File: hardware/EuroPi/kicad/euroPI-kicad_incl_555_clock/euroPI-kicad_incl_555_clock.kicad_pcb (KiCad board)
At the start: 2 copper layers, 121.9 x 128.5 mm, 104 parts, among them J1 Output 1 Jack, J10 Eurorack Power 2x8 16p, J11 Conn_01x13_Socket, J12 OLED 64x128, J13 USB_B_Micro, J14 Conn_01x03_Pin, J15 Conn_01x04_Pin, J16 Conn_02x04_Top_Bottom, J17 Conn_01x13_Pin, J18 Conn_01x04_Pin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

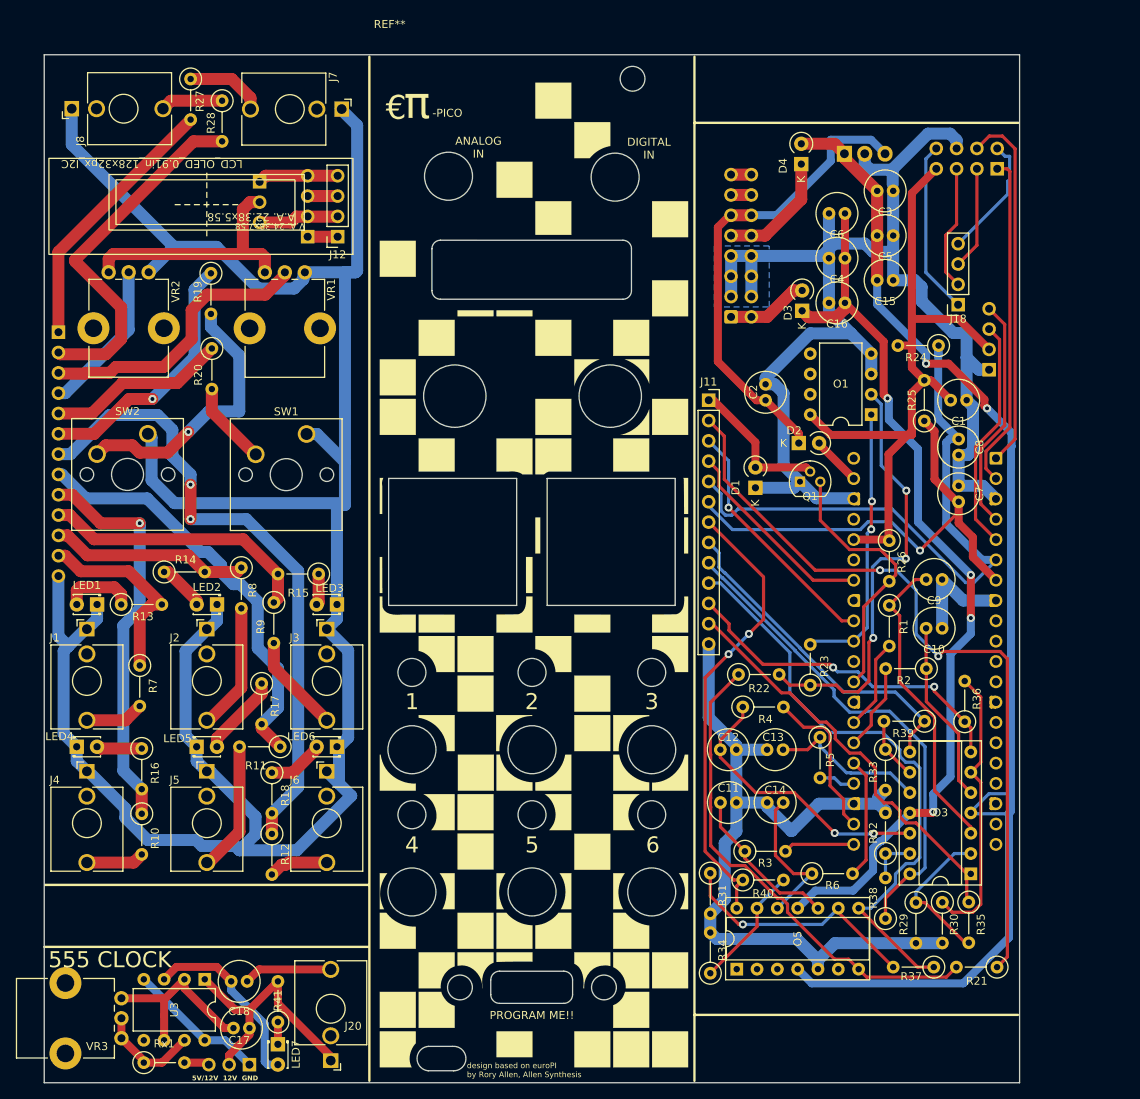
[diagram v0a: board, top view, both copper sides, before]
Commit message: THT version updated with ground plane
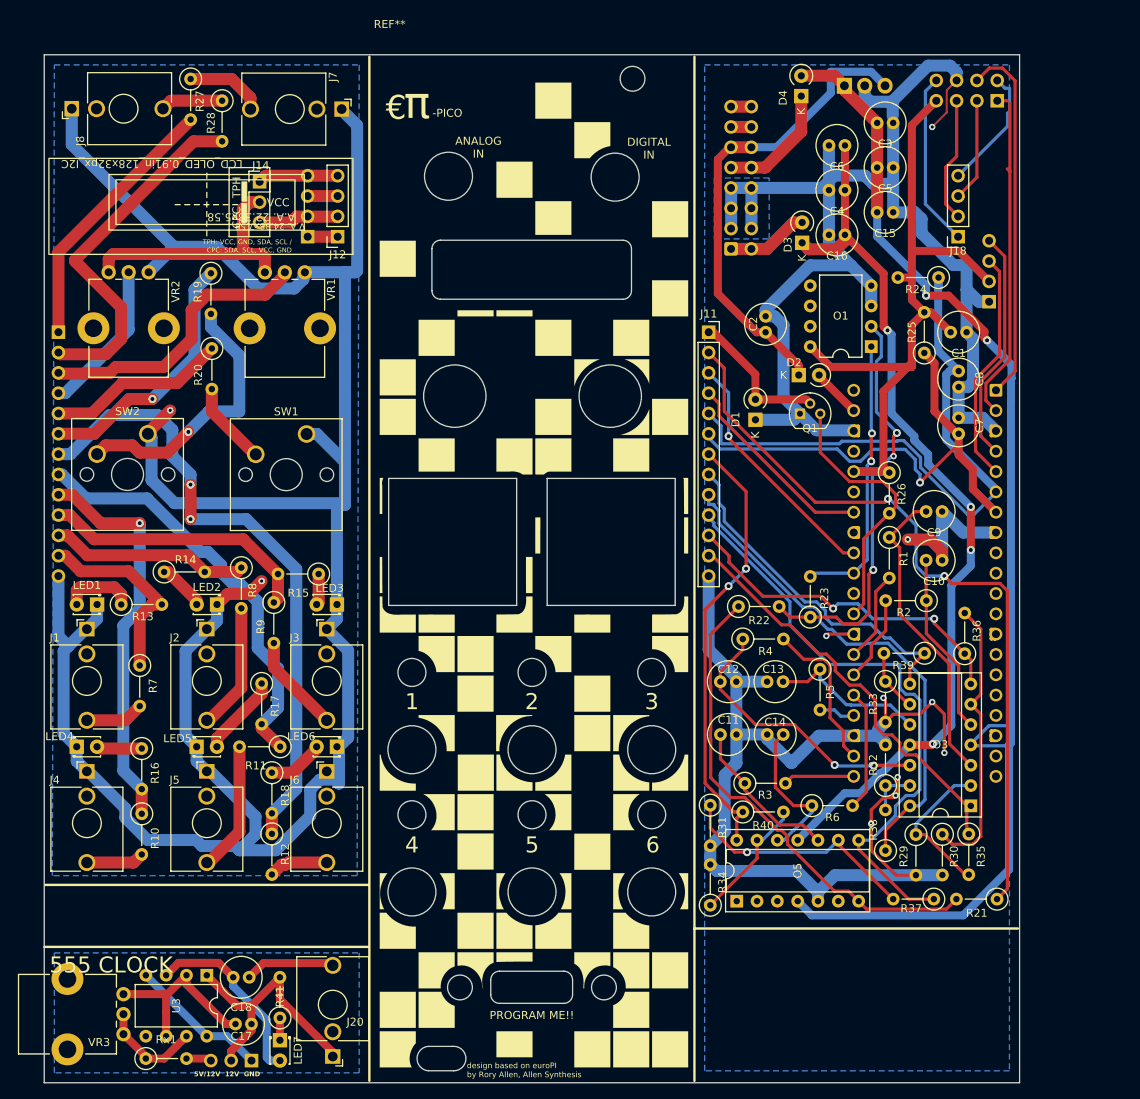
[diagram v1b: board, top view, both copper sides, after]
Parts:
- J14: moved to F.Cu
- moved R38 8.50 mm to (186.4, 124.9)
- moved R40 8.50 mm to (168.6, 120.1)
- moved R25 8.50 mm to (191.3, 62.7)
- moved D4 8.50 mm to (175.9, 30.6)
- moved U1 8.50 mm to (181.3, 29.3)
- moved C1 8.50 mm to (194.6, 60.1)
- moved C10 8.50 mm to (191.5, 88.6)
- moved C11 8.50 mm to (165.8, 110.4)
- moved C12 8.50 mm to (165.8, 103.8)
- moved C13 8.50 mm to (173.6, 103.8)
- moved C14 8.50 mm to (173.7, 110.4)
- moved C15 8.50 mm to (185.4, 45.1)
- moved C16 8.50 mm to (179.4, 47.9)
- moved C2 8.50 mm to (171.4, 60.1)
- moved C3 8.50 mm to (185.4, 33.9)
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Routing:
- net I2C_GND: track 610.0 -> 671.9 mm, vias 0 -> 11
- net I2C_VCC: track 117.6 -> 121.8 mm
- net Net-(O1A--): track 54.2 -> 52.0 mm
- net CJ6: track 136.6 -> 134.5 mm
- net CS2: track 94.2 -> 95.9 mm
- net CJ5: track 95.0 -> 96.6 mm
- net -12V: track 114.9 -> 113.3 mm
- net CJ4: track 111.3 -> 112.9 mm
- net CJ3: track 108.3 -> 109.4 mm
- net CS1: track 100.5 -> 100.0 mm
- net Net-(O5D-+): track 18.6 -> 19.1 mm

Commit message: wip tried a reroute should move power rail caps closer i think
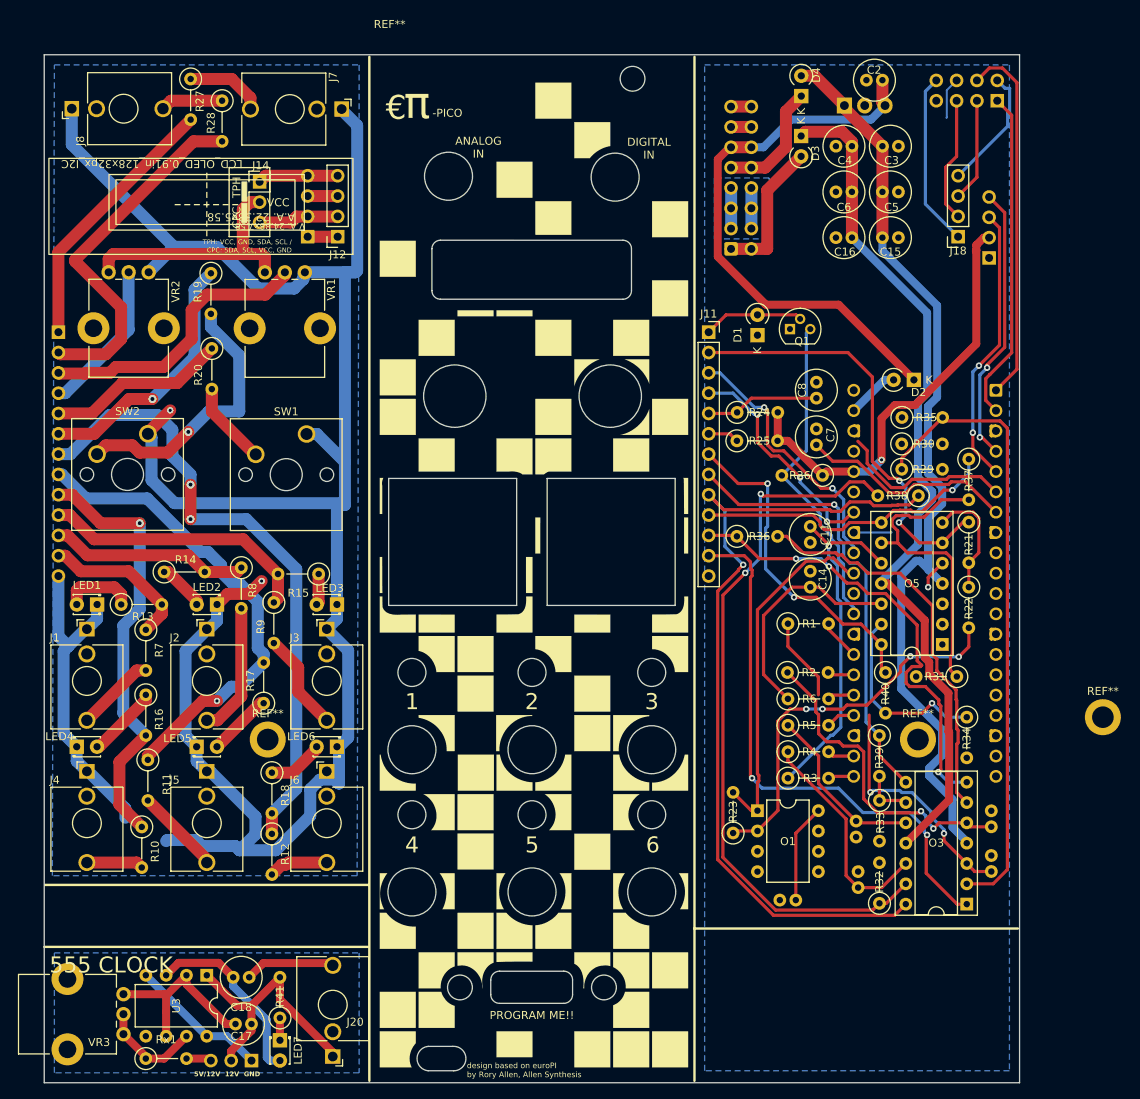
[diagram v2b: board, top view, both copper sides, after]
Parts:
- added REF**: MountingHole_2.7mm_M2.5_ISO14580_Pad, MountingHole:MountingHole_2.7mm_M2.5_ISO14580_Pad, F.Cu at (109.2, 111.0)
- added REF**: MountingHole_2.7mm_M2.5_ISO14580_Pad, MountingHole:MountingHole_2.7mm_M2.5_ISO14580_Pad, F.Cu at (213.6, 108.2)
- added REF**: MountingHole_2.7mm_M2.5_ISO14580_Pad, MountingHole:MountingHole_2.7mm_M2.5_ISO14580_Pad, F.Cu at (190.5, 111.0)
- C1, C10, C12, C13, C9: moved to B.Cu
- D1, D2, D3, D4: value type="D" model="DIODE" lib="" -> 1n4001
- moved C1 73.6 mm to (175.2, 131.1), turned to 180 degrees
- moved O1 59.7 mm to (170.4, 119.9), turned to 0 degrees
- moved R37 55.2 mm to (196.8, 75.9), turned to -90 degrees
- moved R35 52.7 mm to (188.5, 70.7), turned to 0 degrees
- moved R30 49.1 mm to (188.5, 74.0), turned to 0 degrees
- moved R21 47.3 mm to (196.8, 83.8), turned to -90 degrees
- moved C9 45.7 mm to (199.7, 127.5), turned to 90 degrees
- moved R29 45.7 mm to (188.5, 77.2), turned to 0 degrees
- moved R38 44.5 mm to (190.6, 80.5), turned to 180 degrees
- moved O5 41.1 mm to (193.5, 99.1), turned to 180 degrees
- moved R34 39.7 mm to (196.6, 108.2), turned to -90 degrees
- moved R31 34.8 mm to (195.4, 103.1), turned to 180 degrees
- moved C2 34.7 mm to (186.1, 28.6), turned to 180 degrees
- moved C10 34.3 mm to (199.7, 121.9), turned to 90 degrees
- moved R36 32.0 mm to (167.9, 85.6), turned to 0 degrees
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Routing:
- net I2C_GND: track 671.9 -> 355.4 mm, vias 11 -> 3
- net Net-(O3D--): track 6.10 -> 90.5 mm, vias 0 -> 2
- net Net-(O3A--): track 18.9 -> 78.2 mm
- net Net-(O5-Pad7): track 61.5 -> 14.6 mm
- net CJ4: track 112.9 -> 158.1 mm, vias 1 -> 2
- net CJA: track 140.7 -> 98.9 mm
- net CS1: track 100.0 -> 58.8 mm
- net ~: track 172.5 -> 134.7 mm, vias 2 -> 0
- net CJ3: track 109.4 -> 72.7 mm, vias 0 -> 1
- net CS2: track 95.9 -> 63.3 mm, vias 2 -> 1
- net Net-(O5C-+): track 20.0 -> 43.7 mm, vias 0 -> 1
- net I2C_VCC: track 121.8 -> 98.1 mm, vias 0 -> 1
- net CJ5: track 96.6 -> 116.0 mm, vias 0 -> 2
- net Net-(O3B-+): track 22.9 -> 40.3 mm, vias 0 -> 2
- net GP17: track 19.8 -> 3.37 mm
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
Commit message: reorg continued mainly trying to get power filtering better situated
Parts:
- added REF**: C_0805_2012Metric_Pad1.18x1.45mm_HandSolder, Capacitor_SMD:C_0805_2012Metric_Pad1.18x1.45mm_HandSolder, F.Cu at (205.2, 90.9)
- O3, O5: footprint Package_DIP:DIP-14_W7.62mm_Socket -> Library:DIP-14_W7.62mm_Socket_gap_in_the_middle
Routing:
- net (no net): track 0.00 -> 16.6 mm
- net CJA: track 98.9 -> 100.0 mm

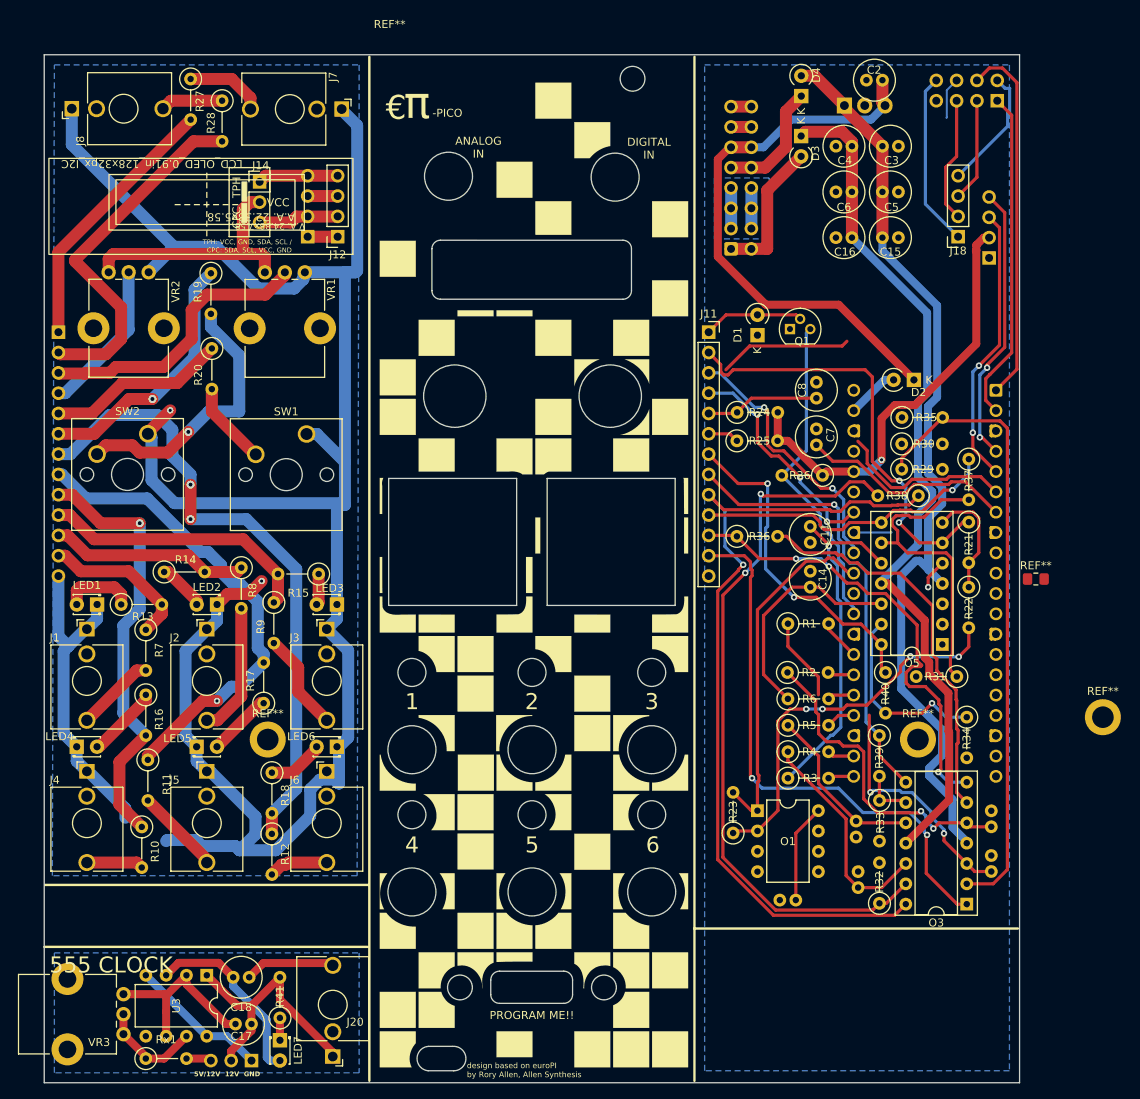
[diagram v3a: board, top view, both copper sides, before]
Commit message: updated with caps under sockets in order to improve power filtering as intended
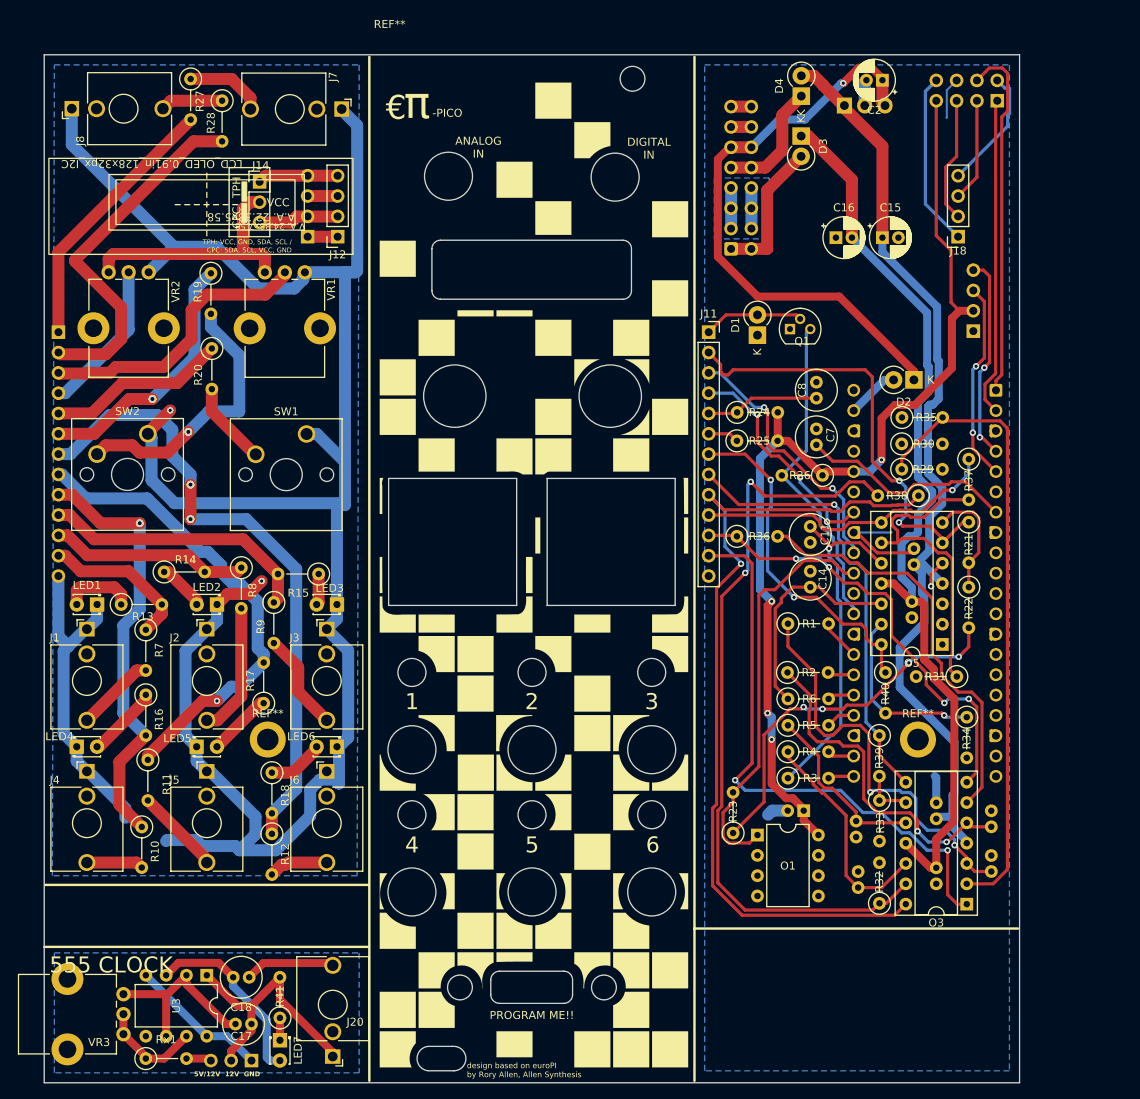
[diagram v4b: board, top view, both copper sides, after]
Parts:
- removed the REF** at (205.2, 90.9)
- removed the REF** at (213.6, 108.2)
- C1, C2: value 1uF -> 1uF (Polarised); footprint Capacitor_THT:C_Radial_D5.0mm_H11.0mm_P2.00mm -> Capacitor_THT:CP_Radial_D5.0mm_P2.00mm
- C15, C16: value 10uF -> 10uF (Polarised); footprint Capacitor_THT:C_Radial_D5.0mm_H11.0mm_P2.00mm -> Capacitor_THT:CP_Radial_D5.0mm_P2.00mm
- C3, C4, C5, C6: moved to B.Cu
- D1, D2, D3, D4: value 1n4001 -> 1N5817 Schottky Diode; footprint Diode_THT:D_A-405_P2.54mm_Vertical_KathodeUp -> Diode_THT:D_DO-41_SOD81_P2.54mm_Vertical_KathodeUp
- moved C6 87.4 mm to (192.8, 129.0), turned to 90 degrees
- moved C5 78.6 mm to (192.8, 120.9), turned to 90 degrees
- moved C4 59.7 mm to (189.7, 95.8), turned to 90 degrees
- moved C3 52.5 mm to (190.0, 89.1), turned to 90 degrees
- moved C1 11.2 mm to (176.2, 119.9)
- moved J15 9.35 mm to (197.4, 59.9)
- moved O1 3.05 mm to (170.4, 122.9)
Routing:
- net I2C_VCC: track 98.1 -> 158.0 mm, vias 1 -> 4
- net CS1: track 58.8 -> 36.8 mm
- net I2C_GND: track 355.4 -> 373.3 mm
- net (no net): track 16.6 -> 0.00 mm
- net Net-(O3A-+): track 40.8 -> 51.5 mm
- net GP3: track 34.9 -> 25.0 mm
- net GP2: track 34.9 -> 25.7 mm
- net -12V: track 108.7 -> 116.0 mm
- net GP26: track 44.7 -> 51.4 mm
- net Net-(O3D--): track 90.5 -> 96.2 mm
- net +5V: track 73.4 -> 76.4 mm, vias 0 -> 1
- net Net-(O3B--): track 49.5 -> 52.4 mm
- net CJ1: track 88.9 -> 91.9 mm
- net CJ4: track 158.1 -> 160.7 mm
- net Net-(O3B-+): track 40.3 -> 42.7 mm
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
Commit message: extra standoff :)
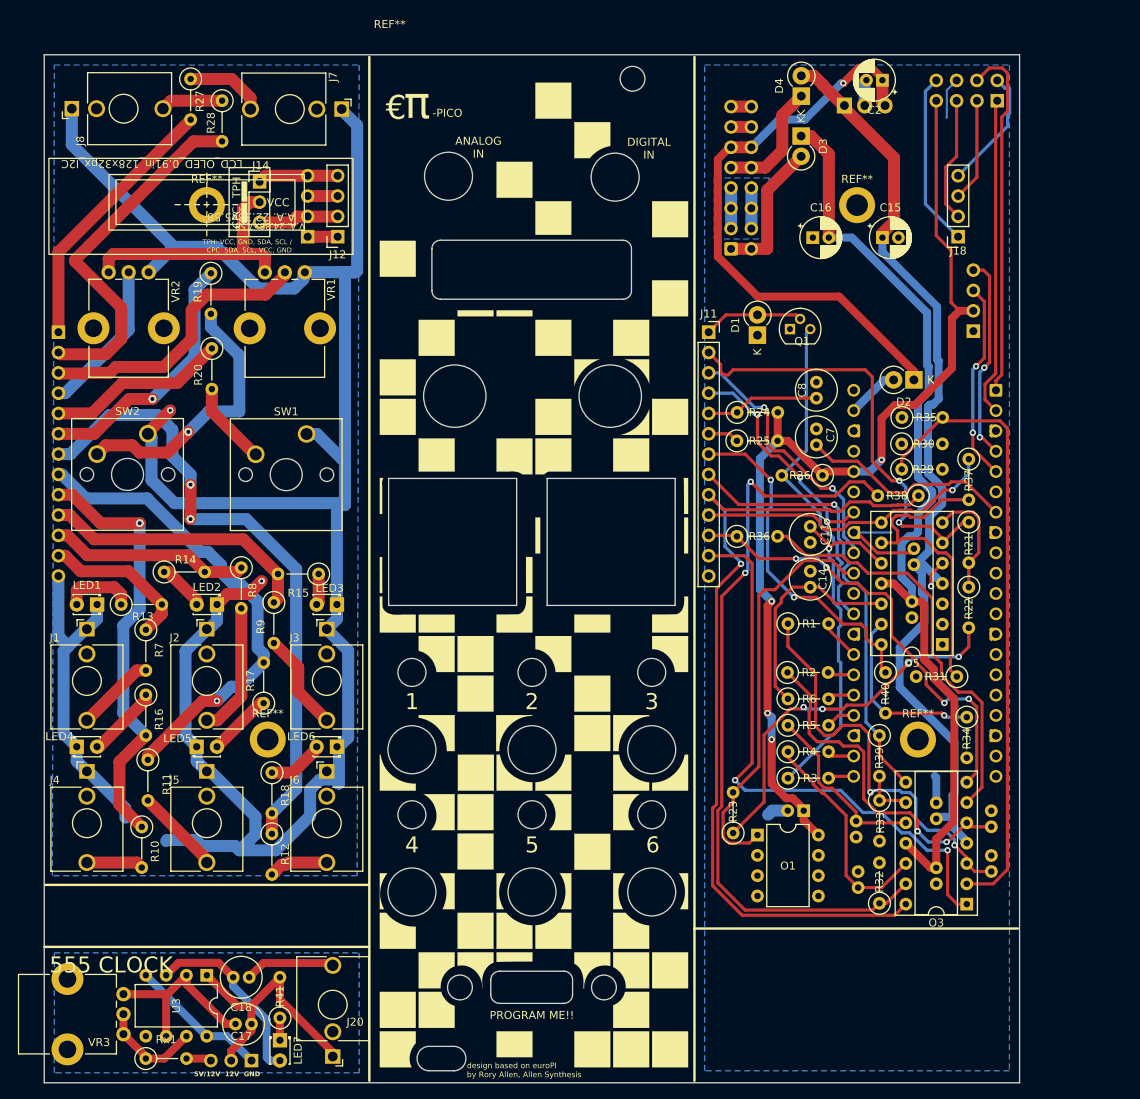
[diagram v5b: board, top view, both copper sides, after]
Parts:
- added REF**: MountingHole_2.7mm_M2.5_ISO14580_Pad, MountingHole:MountingHole_2.7mm_M2.5_ISO14580_Pad, F.Cu at (101.6, 44.2)
- added REF**: MountingHole_2.7mm_M2.5_ISO14580_Pad, MountingHole:MountingHole_2.7mm_M2.5_ISO14580_Pad, F.Cu at (182.9, 44.2)
- moved C16 2.89 mm to (177.4, 48.3)
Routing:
- net -12V: track 116.0 -> 117.9 mm
- net ~: track 136.9 -> 138.1 mm
- net GP22: track 40.8 -> 41.7 mm
- net CJ5: track 116.0 -> 116.6 mm
